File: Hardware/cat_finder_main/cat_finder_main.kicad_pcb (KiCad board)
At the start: 2 copper layers, 85 x 70 mm, 36 parts, among them J1 BATT, J10 Analog, J11 Bast Pin, J2 BME280, J3 CSS811, J4 DRIVERS, J5 GY-87, J6 PROG, J7 FTDI, J8 Digital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

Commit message: move diode
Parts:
- moved D1 13.7 mm to (171.0, 82.8)
- moved U2 5.51 mm to (175.3, 92.6)
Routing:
- net /BATT: track 24.9 -> 13.5 mm
- net VCC: track 143.0 -> 136.5 mm

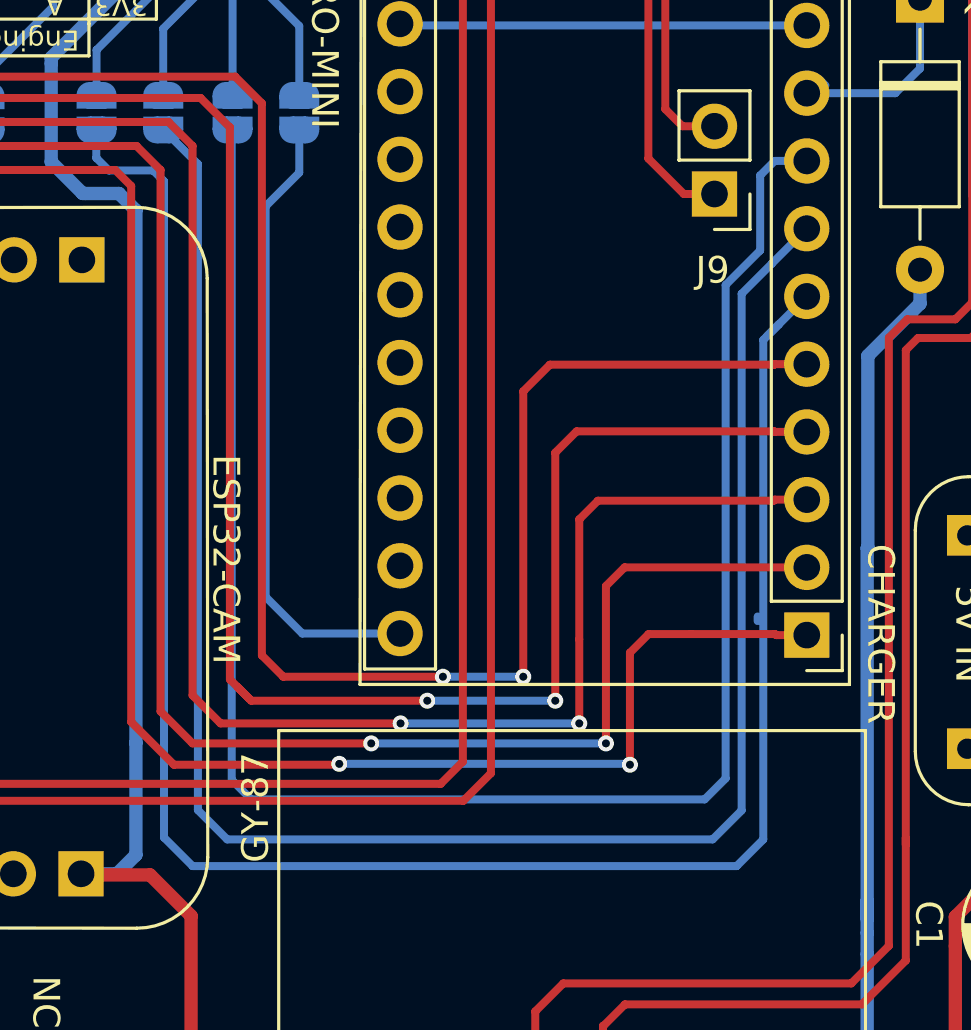
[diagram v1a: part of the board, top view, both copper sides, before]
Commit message: fix conection A1
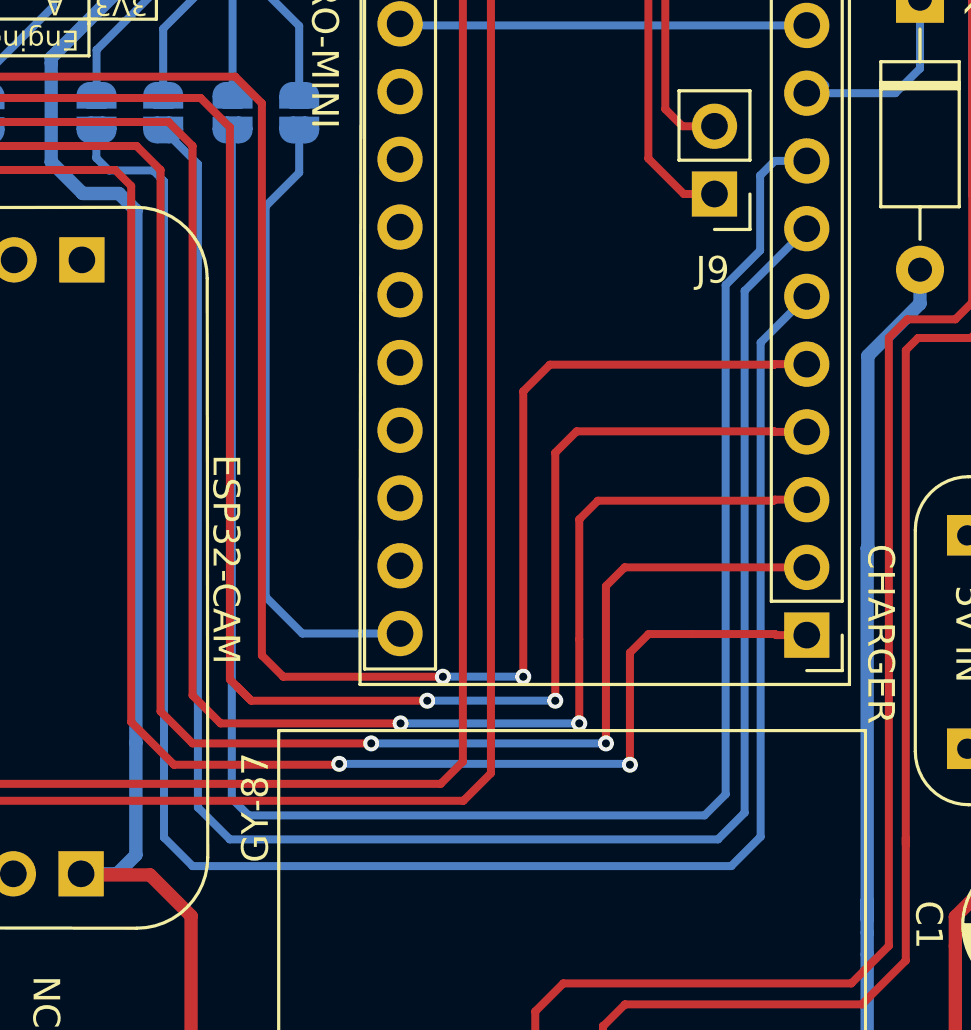
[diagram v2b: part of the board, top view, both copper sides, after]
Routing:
- net /A3: track 68.6 -> 69.9 mm
- net /A1: track 73.7 -> 72.8 mm
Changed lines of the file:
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@@
     (thickness 1.6)
     (drawings 122)
-    (tracks 375)
+    (tracks 370)
     (zones 0)
     (modules 36)
@@
   (segment (start 147.34 69.48) (end 147.28 69.42) (width 0.3) (layer B.Cu) (net 33))
   (segment (start 162.53 69.48) (end 147.34 69.48) (width 0.3) (layer B.Cu) (net 33))
-  (segment (start 140.97 97.77) (end 140.97 96.33) (width 0.3) (layer B.Cu) (net 34))
-  (segment (start 158.7 98.5) (end 141.7 98.5) (width 0.3) (layer B.Cu) (net 34))
+  (segment (start 140.97 96.33) (end 140.97 73.406) (width 0.3) (layer B.Cu) (net 34))
+  (segment (start 140.97 98.47) (end 140.97 96.33) (width 0.3) (layer B.Cu) (net 34))
+  (segment (start 141.6 99.1) (end 140.97 98.47) (width 0.3) (layer B.Cu) (net 34))
+  (segment (start 158.7 99.1) (end 141.6 99.1) (width 0.3) (layer B.Cu) (net 34))
   (segment (start 162.53 74.56) (end 161.327919 74.56) (width 0.3) (layer B.Cu) (net 34))
   (segment (start 161.327919 74.56) (end 160.782 75.105919) (width 0.3) (layer B.Cu) (net 34))
   (segment (start 160.782 75.105919) (end 160.782 77.918) (width 0.3) (layer B.Cu) (net 34))
-  (segment (start 140.97 96.33) (end 140.97 73.406) (width 0.3) (layer B.Cu) (net 34))
-  (segment (start 141.7 98.5) (end 140.97 97.77) (width 0.3) (layer B.Cu) (net 34))
   (segment (start 160.782 77.918) (end 159.48798 79.21202) (width 0.3) (layer B.Cu) (net 34))
-  (segment (start 159.48798 79.21202) (end 159.48798 97.71202) (width 0.3) (layer B.Cu) (net 34))
-  (segment (start 159.48798 97.71202) (end 158.7 98.5) (width 0.3) (layer B.Cu) (net 34))
-  (segment (start 161.215 78.415) (end 162.53 77.1) (width 0.3) (layer B.Cu) (net 35))
-  (segment (start 160.08799 79.54201) (end 161.215 78.415) (width 0.3) (layer B.Cu) (net 35))
+  (segment (start 159.48798 79.21202) (end 159.48798 98.31202) (width 0.3) (layer B.Cu) (net 34))
+  (segment (start 159.48798 98.31202) (end 158.7 99.1) (width 0.3) (layer B.Cu) (net 34))
+  (segment (start 139.7 98.8) (end 140.9 100) (width 0.3) (layer B.Cu) (net 35))
+  (segment (start 139.7 74.676) (end 139.7 98.8) (width 0.3) (layer B.Cu) (net 35))
   (segment (start 138.43 73.406) (end 139.7 74.676) (width 0.3) (layer B.Cu) (net 35))
-  (segment (start 139.7 74.676) (end 139.7 98.9) (width 0.3) (layer B.Cu) (net 35))
-  (segment (start 139.7 98.9) (end 140.8 100) (width 0.3) (layer B.Cu) (net 35))
-  (segment (start 140.8 100) (end 159 100) (width 0.3) (layer B.Cu) (net 35))
-  (segment (start 159 100) (end 160.08799 98.91201) (width 0.3) (layer B.Cu) (net 35))
-  (segment (start 160.08799 98.91201) (end 160.08799 79.54201) (width 0.3) (layer B.Cu) (net 35))
+  (segment (start 162.53 77.1) (end 160.2 79.43) (width 0.3) (layer B.Cu) (net 35))
+  (segment (start 160.2 79.43) (end 160.2 99) (width 0.3) (layer B.Cu) (net 35))
+  (segment (start 159.2 100) (end 140.9 100) (width 0.3) (layer B.Cu) (net 35))
+  (segment (start 160.2 99) (end 159.2 100) (width 0.3) (layer B.Cu) (net 35))
+  (segment (start 160.8 81.37) (end 162.53 79.64) (width 0.3) (layer B.Cu) (net 36))
+  (segment (start 160.8 99.9) (end 160.8 81.37) (width 0.3) (layer B.Cu) (net 36))
+  (segment (start 159.7 101) (end 160.8 99.9) (width 0.3) (layer B.Cu) (net 36))
+  (segment (start 139.5 101) (end 159.7 101) (width 0.3) (layer B.Cu) (net 36))
   (segment (start 135.89 74.4474) (end 136.3599 74.9173) (width 0.3) (layer B.Cu) (net 36))
   (segment (start 136.3599 74.9173) (end 138.0236 74.9173) (width 0.3) (layer B.Cu) (net 36))
-  (segment (start 135.89 73.406) (end 135.89 74.4474) (width 0.3) (layer B.Cu) (net 36))
   (segment (start 138.0236 74.9173) (end 138.43 75.3237) (width 0.3) (layer B.Cu) (net 36))
-  (segment (start 160.688 91.812) (end 160.688 91.642) (width 0.3) (layer B.Cu) (net 36))
-  (segment (start 138.43 98.47) (end 138.43 99.93) (width 0.3) (layer B.Cu) (net 36))
-  (segment (start 138.43 75.3237) (end 138.43 98.47) (width 0.3) (layer B.Cu) (net 36))
+  (segment (start 138.43 75.3237) (end 138.43 99.93) (width 0.3) (layer B.Cu) (net 36))
+  (segment (start 135.89 73.406) (end 135.89 74.4474) (width 0.3) (layer B.Cu) (net 36))
   (segment (start 138.43 99.93) (end 139.5 101) (width 0.3) (layer B.Cu) (net 36))
-  (segment (start 139.5 101) (end 159.9 101) (width 0.3) (layer B.Cu) (net 36))
-  (segment (start 159.9 101) (end 160.9 100) (width 0.3) (layer B.Cu) (net 36))
-  (segment (start 160.9 81.27) (end 161.485 80.685) (width 0.3) (layer B.Cu) (net 36))
-  (segment (start 160.9 100) (end 160.9 81.27) (width 0.3) (layer B.Cu) (net 36))
-  (segment (start 161.035 81.135) (end 161.485 80.685) (width 0.3) (layer B.Cu) (net 36))
-  (segment (start 161.485 80.685) (end 162.53 79.64) (width 0.3) (layer B.Cu) (net 36))
   (segment (start 161.327919 82.18) (end 161.307919 82.2) (width 0.3) (layer F.Cu) (net 37))
   (segment (start 162.53 82.18) (end 161.327919 82.18) (width 0.3) (layer F.Cu) (net 37))

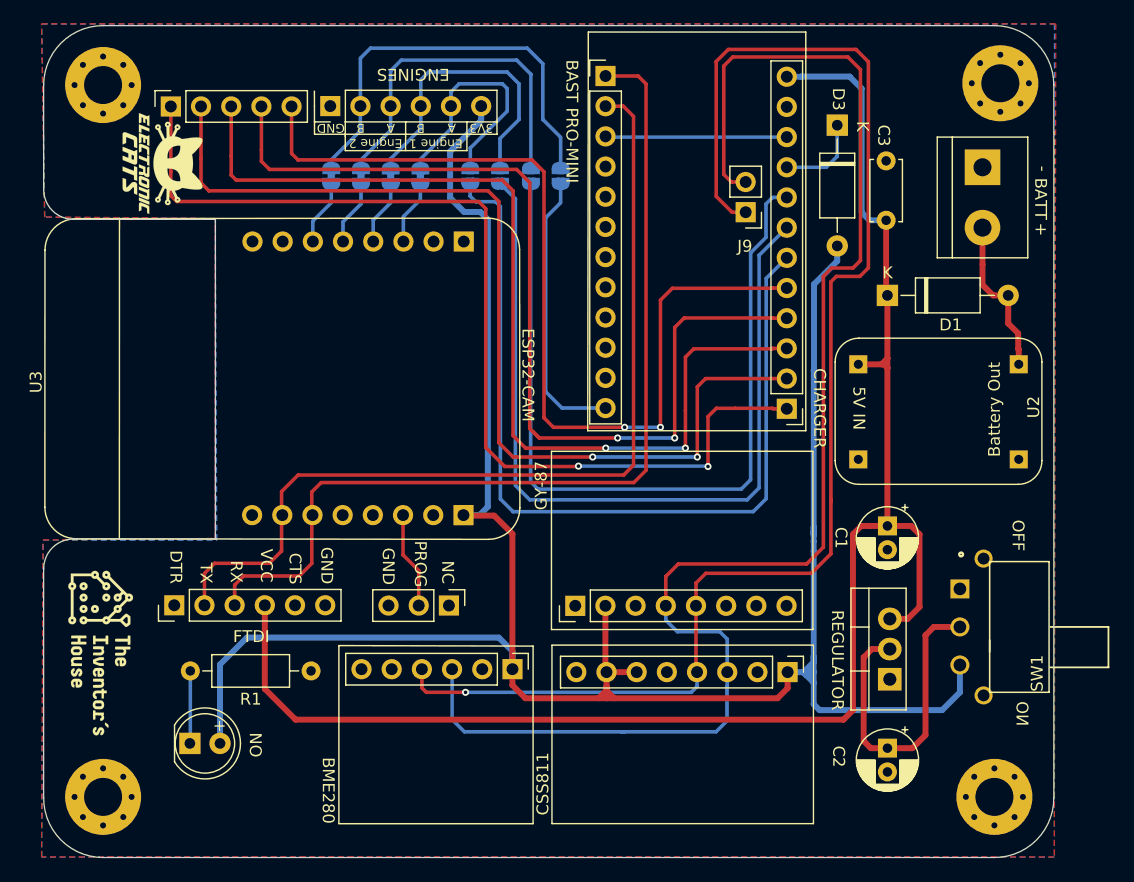
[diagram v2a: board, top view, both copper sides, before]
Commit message: add diode VCC
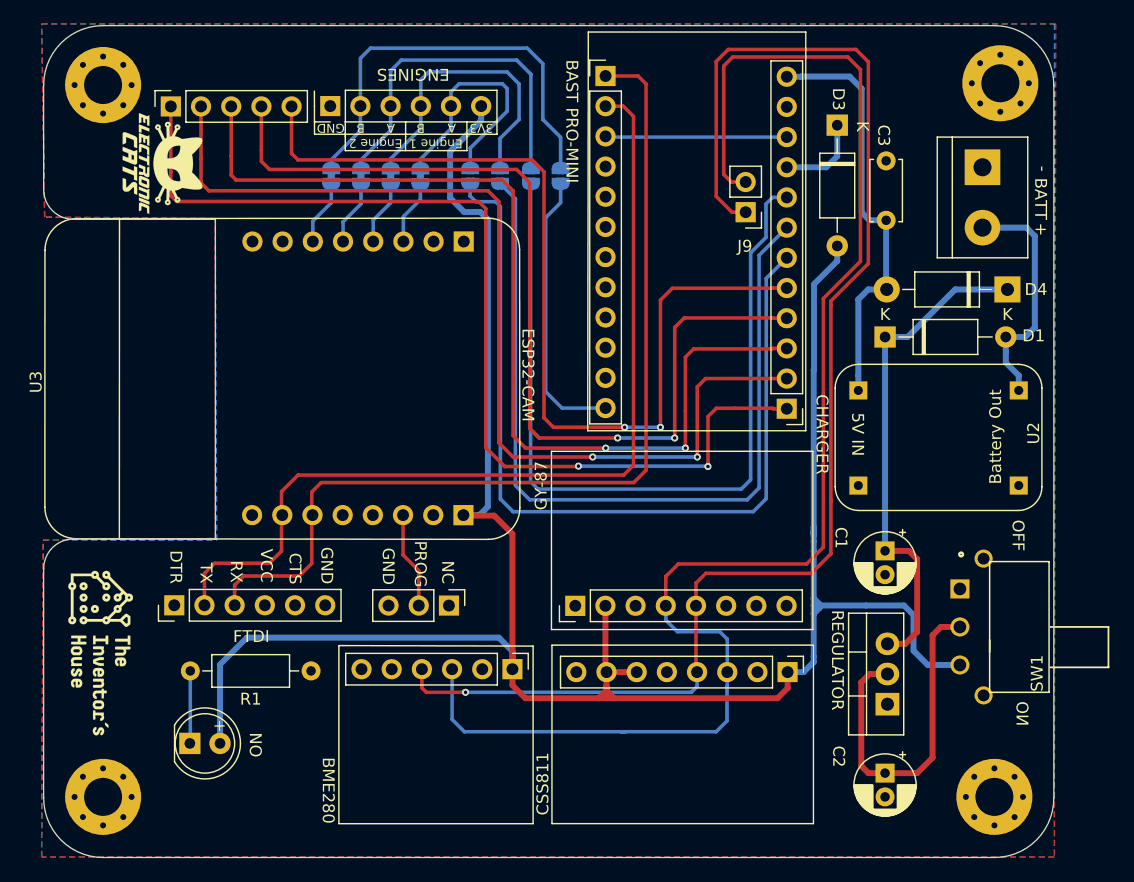
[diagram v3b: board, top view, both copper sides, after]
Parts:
- added D4: D_Schottky, Diode_THT:D_DO-41_SOD81_P10.16mm_Horizontal, F.Cu at (181.1, 82.3)
- moved D1 3.51 mm to (170.8, 86.3)
- moved U2 2.20 mm to (175.3, 94.8)
- moved U1 2.11 mm to (171.0, 117.2)
- moved C1 2.11 mm to (170.8, 104.3)
- moved C2 2.11 mm to (170.8, 123.0)
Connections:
- C1 pad 1: VCC -> Net-(C1-Pad1)
- D1 pad 1: VCC -> Net-(C1-Pad1)
- J7 pad 4: VCC -> Net-(J7-Pad4)
- U1 pad 3: VCC -> Net-(C1-Pad1)
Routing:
- net VCC: track 136.5 -> 35.7 mm
- net Net-(C1-Pad1): track 0.00 -> 42.0 mm
- net /BATT: track 13.5 -> 20.1 mm
- net +3V3: track 189.6 -> 186.0 mm
- net Net-(C2-Pad1): track 27.0 -> 29.2 mm
- net /SDA: track 118.4 -> 117.2 mm
- net /SCL: track 125.2 -> 124.1 mm

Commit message: move tracks
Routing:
- net /SCL: track 124.1 -> 111.9 mm
- net /SDA: track 117.2 -> 109.9 mm, vias 1 -> 0
- net +3V3: track 186.0 -> 182.4 mm

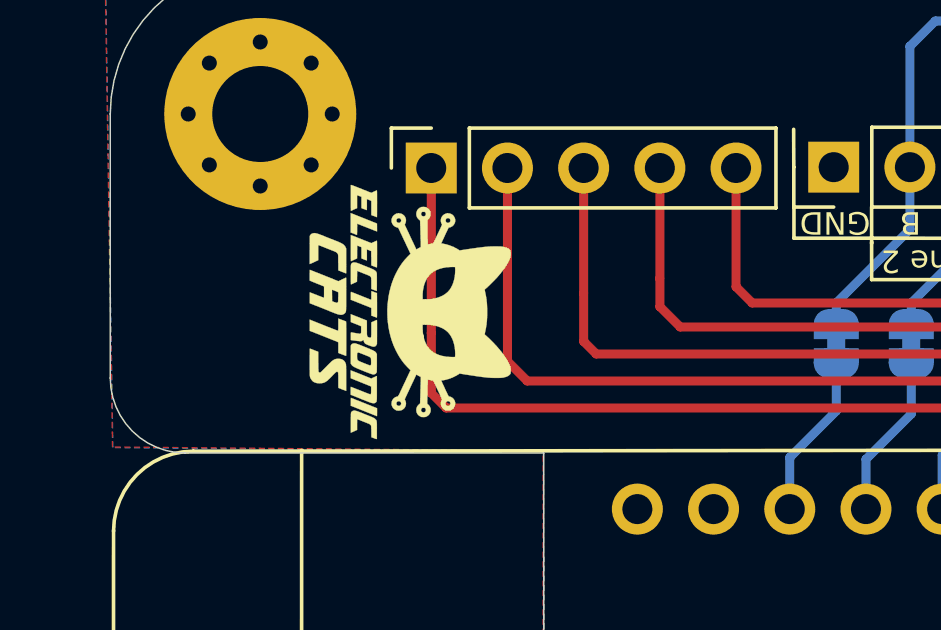
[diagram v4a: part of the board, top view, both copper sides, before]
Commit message: add labels
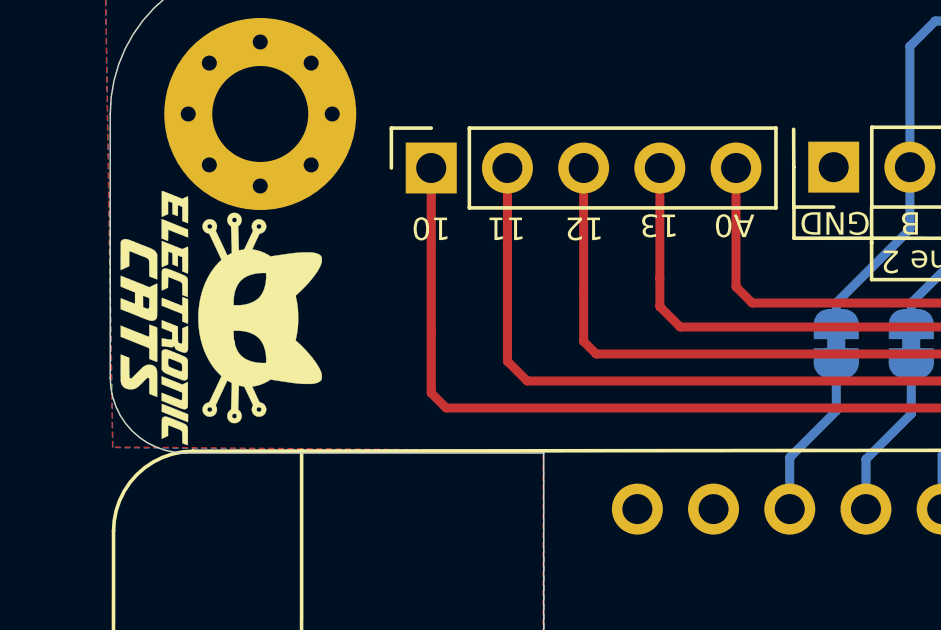
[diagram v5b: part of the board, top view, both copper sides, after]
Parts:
- moved G*** 6.30 mm to (103.7, 71.9)
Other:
- board text added: "10"
- board text added: "11"
- board text added: "12"
- board text added: "13"
- board text added: "A0"
- board text removed: "I2C BAST"
- board text removed: "I2C ESP"
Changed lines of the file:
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@@
   (general
     (thickness 1.6)
-    (drawings 122)
+    (drawings 125)
     (tracks 358)
     (zones 0)
@@
   )
   (module Aesthetics:electronic_cats_logo_8x6 (layer F.Cu)
-    (at 110 71.7 270)
+    (at 103.7 71.9 270)
     (fp_text reference G*** (at 0 0 270) (layer F.SilkS) hide
       (effects (font (size 1.524 1.524) (thickness 0.3)))
@@
     )
   )
+  (gr_text 10 (at 110.7 68.9 180) (layer F.SilkS)
+    (effects (font (size 0.75 0.75) (thickness 0.15)))
+  )
+  (gr_text 11 (at 113.2 68.9 180) (layer F.SilkS)
+    (effects (font (size 0.75 0.75) (thickness 0.15)))
+  )
+  (gr_text 12 (at 115.8 68.9 180) (layer F.SilkS)
+    (effects (font (size 0.75 0.75) (thickness 0.15)))
+  )
+  (gr_text 13 (at 118.3 68.8 180) (layer F.SilkS)
+    (effects (font (size 0.75 0.75) (thickness 0.15)))
+  )
+  (gr_text A0 (at 120.8 68.8 180) (layer F.SilkS)
+    (effects (font (size 0.75 0.75) (thickness 0.15)))
+  )
   (gr_text OFF (at 182 103 270) (layer F.SilkS)
     (effects (font (size 1 1) (thickness 0.15)))
@@
     (effects (font (size 1 1) (thickness 0.15)))
   )
-  (gr_text "I2C BAST" (at 153.416 106.934) (layer B.SilkS)
-    (effects (font (size 1 1) (thickness 0.15)) (justify mirror))
-  )
-  (gr_text "I2C ESP" (at 139.573 107.061) (layer B.SilkS)
-    (effects (font (size 1 1) (thickness 0.15)) (justify mirror))
-  )
   (gr_text "DRIVERS BAST" (at 139.827 70.358) (layer B.SilkS)
     (effects (font (size 1 1) (thickness 0.15)) (justify mirror))
@@
   (segment (start 169.384366 82.3) (end 168.55 83.134366) (width 0.5) (layer B.Cu) (net 3))
   (segment (start 170.94 82.3) (end 169.384366 82.3) (width 0.5) (layer B.Cu) (net 3))
-  (segment (start 172.5 112.12) (end 171 112.12) (width 0.5) (layer F.Cu) (net 54))
-  (segment (start 173.5 111.12) (end 172.5 112.12) (width 0.5) (layer F.Cu) (net 54))
-  (segment (start 173.5 105) (end 173.5 111.12) (width 0.5) (layer F.Cu) (net 54))
-  (segment (start 172.8 104.3) (end 173.5 105) (width 0.5) (layer F.Cu) (net 54))
-  (segment (start 170.8 104.3) (end 172.8 104.3) (width 0.5) (layer F.Cu) (net 54))
   (segment (start 112.34 120.46) (end 112.3 120.5) (width 0.3) (layer B.Cu) (net 4))
   (segment (start 112.34 114.4) (end 112.34 120.46) (width 0.3) (layer B.Cu) (net 4))
@@
   (segment (start 170.8 123) (end 173.5 123) (width 0.5) (layer F.Cu) (net 52))
   (segment (start 175.5 110.7) (end 177.1 110.7) (width 0.5) (layer F.Cu) (net 52))
+  (segment (start 172.5 112.12) (end 171 112.12) (width 0.5) (layer F.Cu) (net 54))
+  (segment (start 173.5 111.12) (end 172.5 112.12) (width 0.5) (layer F.Cu) (net 54))
+  (segment (start 173.5 105) (end 173.5 111.12) (width 0.5) (layer F.Cu) (net 54))
+  (segment (start 172.8 104.3) (end 173.5 105) (width 0.5) (layer F.Cu) (net 54))
+  (segment (start 170.8 104.3) (end 172.8 104.3) (width 0.5) (layer F.Cu) (net 54))
   (segment (start 170.8 86.3) (end 172.7 86.3) (width 0.5) (layer B.Cu) (net 54))
   (segment (start 172.7 86.3) (end 176.7 82.3) (width 0.5) (layer B.Cu) (net 54))
